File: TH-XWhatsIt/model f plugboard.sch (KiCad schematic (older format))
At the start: 4 parts, among them J3 MODEL F PLUGBOARD COLUMNS, J4 MODEL F PLUGBOARD CONNECTOR, J5 MODEL F PLUGBOARD ROWS

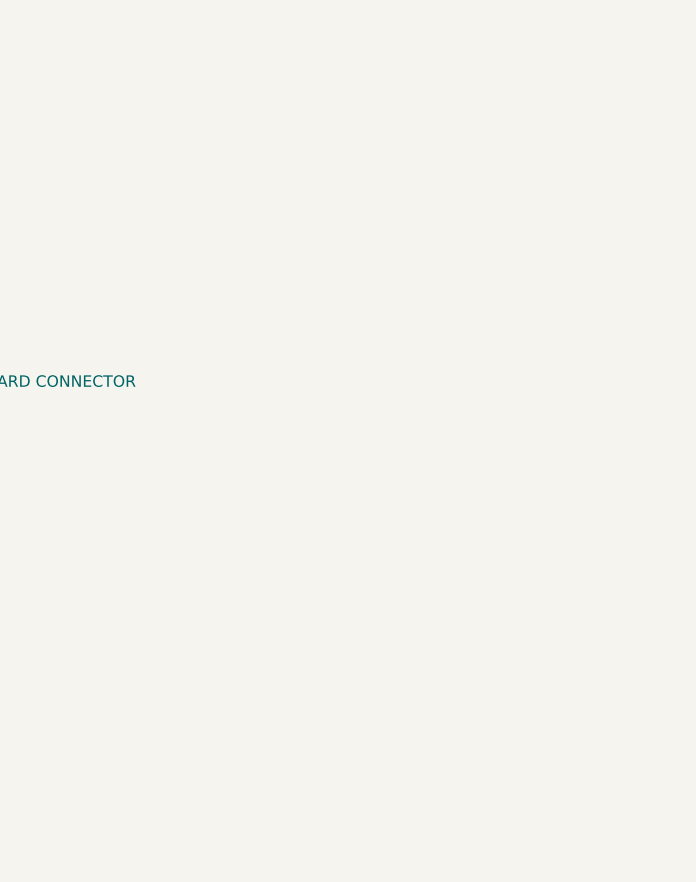
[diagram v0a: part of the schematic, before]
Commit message: model F plugboard: added 3.96 mm connector too
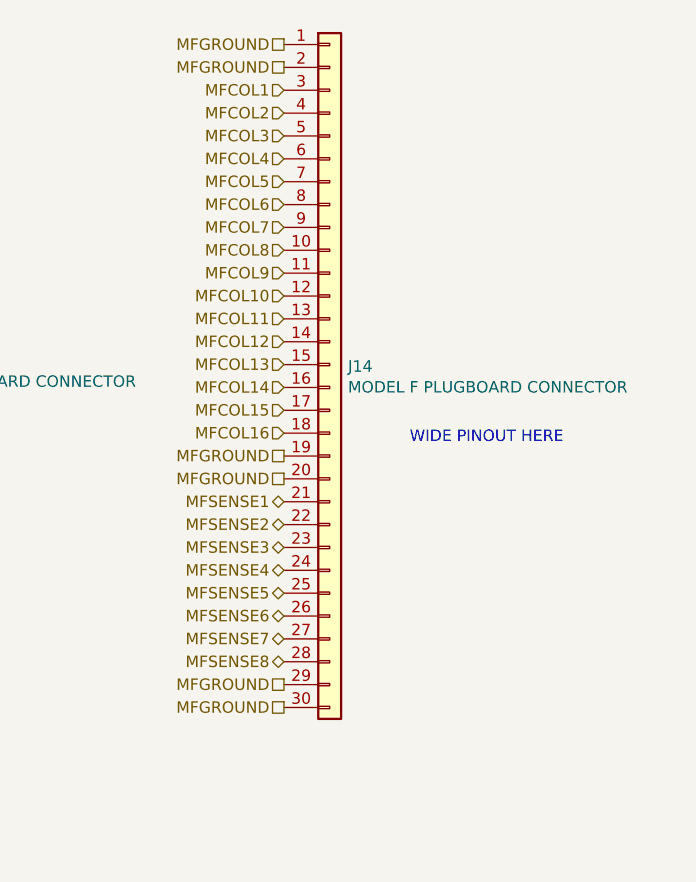
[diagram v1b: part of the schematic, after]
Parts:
- added J14: MODEL F PLUGBOARD CONNECTOR, TH-XWhatsIt:Model_F_3.96mm_pitch_footprint, symbol Connector_Generic:Conn_01x30
- J4: footprint Connector_PinHeader_2.54mm:PinHeader_1x30_P2.54mm_Horizontal -> Connector_PinHeader_2.54mm:PinHeader_1x30_P2.54mm_Vertical
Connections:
- net MFCOL1: now also J14.3 (Pin_3)
- net MFCOL10: now also J14.12 (Pin_12)
- net MFCOL11: now also J14.13 (Pin_13)
- net MFCOL12: now also J14.14 (Pin_14)
- net MFCOL13: now also J14.15 (Pin_15)
- net MFCOL14: now also J14.16 (Pin_16)
- net MFCOL15: now also J14.17 (Pin_17)
- net MFCOL16: now also J14.18 (Pin_18)
- net MFCOL2: now also J14.4 (Pin_4)
- net MFCOL3: now also J14.5 (Pin_5)
- net MFCOL4: now also J14.6 (Pin_6)
- net MFCOL5: now also J14.7 (Pin_7)
- net MFCOL6: now also J14.8 (Pin_8)
- net MFCOL7: now also J14.9 (Pin_9)
- net MFCOL8: now also J14.10 (Pin_10)
- net MFCOL9: now also J14.11 (Pin_11)
- net MFGROUND: now also J14.1 (Pin_1), J14.19 (Pin_19), J14.2 (Pin_2), J14.20 (Pin_20), J14.29 (Pin_29), J14.30 (Pin_30)
- net MFSENSE1: now also J14.21 (Pin_21)
- net MFSENSE2: now also J14.22 (Pin_22)
- net MFSENSE3: now also J14.23 (Pin_23)
- net MFSENSE4: now also J14.24 (Pin_24)
- net MFSENSE5: now also J14.25 (Pin_25)
- net MFSENSE6: now also J14.26 (Pin_26)
- net MFSENSE7: now also J14.27 (Pin_27)
- net MFSENSE8: now also J14.28 (Pin_28)
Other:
- note added: "WIDE PINOUT HERE"
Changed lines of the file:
@@
 F 0 "J4" H 5480 2742 50  0000 L CNN
 F 1 "MODEL F PLUGBOARD CONNECTOR" H 5480 2651 50  0000 L CNN
-F 2 "Connector_PinHeader_2.54mm:PinHeader_1x30_P2.54mm_Horizontal" H 5400 2750 50  0001 C CNN
+F 2 "Connector_PinHeader_2.54mm:PinHeader_1x30_P2.54mm_Vertical" H 5400 2750 50  0001 C CNN
 F 3 "~" H 5400 2750 50  0001 C CNN
 	1    5400 2750
@@
 Text HLabel 5200 5050 3    50   UnSpc ~ 0
 MFGROUND
+$Comp
+L Connector_Generic:Conn_01x30 J14
+U 1 1 5F4406B3
+P 7550 2775
+F 0 "J14" H 7630 2767 50  0000 L CNN
+F 1 "MODEL F PLUGBOARD CONNECTOR" H 7630 2676 50  0000 L CNN
+F 2 "TH-XWhatsIt:Model_F_3.96mm_pitch_footprint" H 7550 2775 50  0001 C CNN
+F 3 "~" H 7550 2775 50  0001 C CNN
+	1    7550 2775
+	1    0    0    -1
+$EndComp
+Text HLabel 7350 1375 0    50   UnSpc ~ 0
+MFGROUND
+Text HLabel 7350 1475 0    50   UnSpc ~ 0
+MFGROUND
+Text HLabel 7350 1575 0    50   Input ~ 0
+MFCOL1
+Text HLabel 7350 1675 0    50   Input ~ 0
+MFCOL2
+Text HLabel 7350 1775 0    50   Input ~ 0
+MFCOL3
+Text HLabel 7350 1875 0    50   Input ~ 0
+MFCOL4
+Text HLabel 7350 1975 0    50   Input ~ 0
+MFCOL5
+Text HLabel 7350 2075 0    50   Input ~ 0
+MFCOL6
+Text HLabel 7350 2175 0    50   Input ~ 0
+MFCOL7
+Text HLabel 7350 2275 0    50   Input ~ 0
+MFCOL8
+Text HLabel 7350 2375 0    50   Input ~ 0
+MFCOL9
+Text HLabel 7350 2475 0    50   Input ~ 0
+MFCOL10
+Text HLabel 7350 2575 0    50   Input ~ 0
+MFCOL11
+Text HLabel 7350 2675 0    50   Input ~ 0
+MFCOL12
+Text HLabel 7350 2775 0    50   Input ~ 0
+MFCOL13
+Text HLabel 7350 2875 0    50   Input ~ 0
+MFCOL14
+Text HLabel 7350 2975 0    50   Input ~ 0
+MFCOL15
+Text HLabel 7350 3075 0    50   Input ~ 0
+MFCOL16
+Text HLabel 7350 3175 0    50   UnSpc ~ 0
+MFGROUND
+Text HLabel 7350 3275 0    50   UnSpc ~ 0
+MFGROUND
+Text HLabel 7350 3375 0    50   BiDi ~ 0
+MFSENSE1
+Text HLabel 7350 3475 0    50   BiDi ~ 0
+MFSENSE2
+Text HLabel 7350 3575 0    50   BiDi ~ 0
+MFSENSE3
+Text HLabel 7350 3675 0    50   BiDi ~ 0
+MFSENSE4
+Text HLabel 7350 3775 0    50   BiDi ~ 0
+MFSENSE5
+Text HLabel 7350 3875 0    50   BiDi ~ 0
+MFSENSE6
+Text HLabel 7350 3975 0    50   BiDi ~ 0
+MFSENSE7
+Text HLabel 7350 4075 0    50   BiDi ~ 0
+MFSENSE8
+Text HLabel 7350 4175 0    50   UnSpc ~ 0
+MFGROUND
+Text HLabel 7350 4275 0    50   UnSpc ~ 0
+MFGROUND
+Text Notes 7900 3125 0    50   ~ 0
+WIDE PINOUT HERE
 $EndSCHEMATC

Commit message: Various changes to revision 0.1.1
General:
    Made mounting hole bigger (M3). And moved it a little bit so it doesn't interfere with some components.
    Star ground turned into single ground.
    Ground fills added everywhere.
    Many stitching vias added everywhere.
    Added JLCJLCJLCJLC magic string under pro micro. When ordering from JLCPCB, you can select for Order Number: "Specify Location"
    Bumped version number to 0.1.1
    Added silkscreen to mark rows/columns everywhere.
    Added optional holes for soldering grounding wires everywhere.
Controller:
    Added silkscreen to ease debugging, by marking various important nets.
    Rearranged some traces to maintain better separation between traces, and better ground reference.
Model F plugboard:
    Modified 3.96mm pitch holes, to hole sizes and pad sizes that match original xwhatsit model F controller
    Moved 3.96mm pitch holes closer to the edge, so it doesn't interfere with case in F AT cases.
    Added mounting holes
    Added holes to support 3178 keyboards.
Displaywriter:
    Addes support for more connector types. (The displaywriter daughterboard is now taller)
Beamspring:
    Bugfix to a mistake that only affected people that ran update footprints from library.
Beamship daughterboard:
    Added support for more connectors. Added breakoff-able mounting hole.
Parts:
- removed H2: GROUND STRAP, MountingHole:MountingHole_2.2mm_M2_Pad_Via, symbol Mechanical:MountingHole_Pad
- added H10: Left Mountinghole, TH-XWhatsIt:ModelF_new_mounting_hole_left, symbol Mechanical:MountingHole_Pad
- added H11: Right Mountinghole, TH-XWhatsIt:ModelF_new_mounting_hole_right, symbol Mechanical:MountingHole_Pad
- added H7: Solderable ground strap, TH-XWhatsIt:ChassisGnd, symbol Mechanical:MountingHole_Pad
- added J16: MODEL F PLUGBOARD CONNECTOR, TH-XWhatsIt:Model_F_3.96mm_pitch_footprint, symbol Connector_Generic:Conn_01x30
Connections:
- net MFCOL10: now also J16.15 (Pin_15)
- net MFCOL11: now also J16.16 (Pin_16)
- net MFCOL12: now also J16.17 (Pin_17)
- net MFCOL13: now also J16.18 (Pin_18)
- net MFCOL14: now also J16.19 (Pin_19)
- net MFCOL15: now also J16.20 (Pin_20)
- net MFCOL16: now also J16.21 (Pin_21)
- net MFCOL5: now also J16.10 (Pin_10)
- net MFCOL6: now also J16.11 (Pin_11)
- net MFCOL7: now also J16.12 (Pin_12)
- net MFCOL8: now also J16.13 (Pin_13)
- net MFCOL9: now also J16.14 (Pin_14)
- net MFGROUND: now also H10.1, H11.1, H7.1, J16.1 (Pin_1), J16.2 (Pin_2), J16.22 (Pin_22), J16.3 (Pin_3), J16.4 (Pin_4), J16.5 (Pin_5), J16.6 (Pin_6), J16.7 (Pin_7), J16.8 (Pin_8), J16.9 (Pin_9)
- net MFSENSE1: now also J16.23 (Pin_23)
- net MFSENSE2: now also J16.24 (Pin_24)
- net MFSENSE3: now also J16.25 (Pin_25)
- net MFSENSE4: now also J16.26 (Pin_26)
- net MFSENSE5: now also J16.27 (Pin_27)
- net MFSENSE6: now also J16.28 (Pin_28)
- net MFSENSE7: now also J16.29 (Pin_29)
- net MFSENSE8: now also J16.30 (Pin_30)
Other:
- note added: "IBM 3178\n"
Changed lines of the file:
@@
 Copyright Rainy Day Plans.\nThis documentation describes Open Hardware and is licensed under the\nCERN OHL v. 1.2.\nYou may redistribute and modify this documentation under the terms of the\nCERN OHL v.1.2. (http://ohwr.org/cernohl). This documentation is distributed\nWITHOUT ANY EXPRESS OR IMPLIED WARRANTY, INCLUDING OF\nMERCHANTABILITY, SATISFACTORY QUALITY AND FITNESS FOR A\nPARTICULAR PURPOSE. Please see the CERN OHL v.1.2 for applicable\nconditions
-$Comp
-L Mechanical:MountingHole_Pad H2
-U 1 1 5E39F8A0
-P 5200 4950
-F 0 "H2" H 5300 4999 50  0000 L CNN
-F 1 "GROUND STRAP" H 5300 4908 50  0000 L CNN
-F 2 "MountingHole:MountingHole_2.2mm_M2_Pad_Via" H 5200 4950 50  0001 C CNN
-F 3 "~" H 5200 4950 50  0001 C CNN
-	1    5200 4950
-	1    0    0    -1
-$EndComp
-Text HLabel 5200 5050 3    50   UnSpc ~ 0
-MFGROUND
 $Comp
 L Connector_Generic:Conn_01x30 J14
@@
 Text Notes 7900 3125 0    50   ~ 0
 WIDE PINOUT HERE
+$Comp
+L Mechanical:MountingHole_Pad H7
+U 1 1 5FBD8F2F
+P 5700 5350
+F 0 "H7" H 5800 5399 50  0000 L CNN
+F 1 "Solderable ground strap" H 5800 5308 50  0000 L CNN
+F 2 "TH-XWhatsIt:ChassisGnd" H 5700 5350 50  0001 C CNN
+F 3 "~" H 5700 5350 50  0001 C CNN
+	1    5700 5350
+	1    0    0    -1
+$EndComp
+Text HLabel 5700 5450 3    50   UnSpc ~ 0
+MFGROUND
+$Comp
+L Mechanical:MountingHole_Pad H10
+U 1 1 5FBE55BC
+P 6275 5700
+F 0 "H10" H 6375 5749 50  0000 L CNN
+F 1 "Left Mountinghole" H 6375 5658 50  0000 L CNN
+F 2 "TH-XWhatsIt:ModelF_new_mounting_hole_left" H 6275 5700 50  0001 C CNN
+F 3 "~" H 6275 5700 50  0001 C CNN
+	1    6275 5700
+	1    0    0    -1
+$EndComp
+$Comp
+L Mechanical:MountingHole_Pad H11
+U 1 1 5FBE5981
+P 6875 6000
+F 0 "H11" H 6975 6049 50  0000 L CNN
+F 1 "Right Mountinghole" H 6975 5958 50  0000 L CNN
+F 2 "TH-XWhatsIt:ModelF_new_mounting_hole_right" H 6875 6000 50  0001 C CNN
+F 3 "~" H 6875 6000 50  0001 C CNN
+	1    6875 6000
+	1    0    0    -1
+$EndComp
+Text HLabel 6275 5800 3    50   UnSpc ~ 0
+MFGROUND
+Text HLabel 6875 6100 3    50   UnSpc ~ 0
+MFGROUND
+Text Notes 10150 4800 0    50   ~ 0
+IBM 3178\n
+$Comp
+L Connector_Generic:Conn_01x30 J16
+U 1 1 5FC4E3EA
+P 9750 4300
+F 0 "J16" H 9830 4292 50  0000 L CNN
+F 1 "MODEL F PLUGBOARD CONNECTOR" H 9830 4201 50  0000 L CNN
+F 2 "TH-XWhatsIt:Model_F_3.96mm_pitch_footprint" H 9750 4300 50  0001 C CNN
+F 3 "~" H 9750 4300 50  0001 C CNN
+	1    9750 4300
+	1    0    0    -1
+$EndComp
+Text HLabel 9550 3700 0    50   UnSpc ~ 0
+MFGROUND
+Text HLabel 9550 3600 0    50   UnSpc ~ 0
+MFGROUND
+Text HLabel 9550 3800 0    50   Input ~ 0
+MFCOL5
+Text HLabel 9550 3900 0    50   Input ~ 0
+MFCOL6
+Text HLabel 9550 4000 0    50   Input ~ 0
+MFCOL7
+Text HLabel 9550 4100 0    50   Input ~ 0
+MFCOL8
+Text HLabel 9550 4200 0    50   Input ~ 0
+MFCOL9
+Text HLabel 9550 4300 0    50   Input ~ 0
+MFCOL10
+Text HLabel 9550 4400 0    50   Input ~ 0
+MFCOL11
+Text HLabel 9550 4500 0    50   Input ~ 0
+MFCOL12
+Text HLabel 9550 4600 0    50   Input ~ 0
+MFCOL13
+Text HLabel 9550 4700 0    50   Input ~ 0
+MFCOL14
+Text HLabel 9550 4800 0    50   Input ~ 0
+MFCOL15
+Text HLabel 9550 4900 0    50   Input ~ 0
+MFCOL16
+Text HLabel 9550 3500 0    50   UnSpc ~ 0
+MFGROUND
+Text HLabel 9550 3400 0    50   UnSpc ~ 0
+MFGROUND
+Text HLabel 9550 5100 0    50   BiDi ~ 0
+MFSENSE1
+Text HLabel 9550 5200 0    50   BiDi ~ 0
+MFSENSE2
+Text HLabel 9550 5300 0    50   BiDi ~ 0
+MFSENSE3
+Text HLabel 9550 5400 0    50   BiDi ~ 0
+MFSENSE4
+Text HLabel 9550 5500 0    50   BiDi ~ 0
+MFSENSE5
+Text HLabel 9550 5600 0    50   BiDi ~ 0
+MFSENSE6
+Text HLabel 9550 5700 0    50   BiDi ~ 0
+MFSENSE7
+Text HLabel 9550 5800 0    50   BiDi ~ 0
+MFSENSE8
+Text HLabel 9550 5000 0    50   UnSpc ~ 0
+MFGROUND
+Text HLabel 9550 3300 0    50   UnSpc ~ 0
+MFGROUND
+Text HLabel 9550 3200 0    50   UnSpc ~ 0
+MFGROUND
+Text HLabel 9550 3100 0    50   UnSpc ~ 0
+MFGROUND
+Text HLabel 9550 3000 0    50   UnSpc ~ 0
+MFGROUND
+Text HLabel 9550 2900 0    50   UnSpc ~ 0
+MFGROUND
 $EndSCHEMATC
